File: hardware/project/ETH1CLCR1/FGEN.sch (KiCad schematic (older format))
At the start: 74 parts, among them U801 ECS-3225SMV-500-GP-TR, U802 REF192, U803 74AHCT1G08, U804 AD5689BRUZ, U805 AD9835, U806 TL072, U807 DG419LDY, U808 AD5453YRMZ, U809 LT1468, U810 LT1468, U811 LT1468

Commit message: PCB layout
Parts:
- added C832, C833, C835: 100n, Capacitor_SMD:C_0603_1608Metric_Pad1.05x0.95mm_HandSolder, symbol Device:C
- renumbered C832 to C834
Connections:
- net +15VF: now also C832.1, C835.1
- net -15VF: now also C833.1
- net AGNDF: now also C832.2, C833.2, C835.2
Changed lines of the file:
@@
 NoConn ~ 10650 2200
 $Comp
-L ETH1CLCR1:-15VF #PWR0871
+L ETH1CLCR1:-15VF #PWR0873
 U 1 1 5DDED26A
 P 10450 2300
-F 0 "#PWR0871" H 10450 2150 50  0001 C CNN
+F 0 "#PWR0873" H 10450 2150 50  0001 C CNN
 F 1 "-15VF" H 10465 2473 50  0000 C CNN
 F 2 "" H 10450 2300 50  0001 C CNN
@@
 	10000 1200 11100 1200
 $Comp
-L ETH1CLCR1:+15VF #PWR0873
+L ETH1CLCR1:+15VF #PWR0877
 U 1 1 5DE564DC
 P 12000 1600
-F 0 "#PWR0873" H 12000 1450 50  0001 C CNN
+F 0 "#PWR0877" H 12000 1450 50  0001 C CNN
 F 1 "+15VF" H 12015 1773 50  0000 C CNN
 F 2 "" H 12000 1600 50  0001 C CNN
@@
 $EndComp
 $Comp
-L ETH1CLCR1:-15VF #PWR0874
+L ETH1CLCR1:-15VF #PWR0878
 U 1 1 5DE5674F
 P 12000 2400
-F 0 "#PWR0874" H 12000 2250 50  0001 C CNN
+F 0 "#PWR0878" H 12000 2250 50  0001 C CNN
 F 1 "-15VF" H 12015 2573 50  0000 C CNN
 F 2 "" H 12000 2400 50  0001 C CNN
@@
 	12550 2000 12500 2000
 $Comp
-L Device:C C832
+L Device:C C834
 U 1 1 5E0264FF
 P 12050 850
-F 0 "C832" V 11798 850 50  0000 C CNN
+F 0 "C834" V 11798 850 50  0000 C CNN
 F 1 "C" V 11889 850 50  0000 C CNN
 F 2 "Capacitor_SMD:C_0603_1608Metric_Pad1.05x0.95mm_HandSolder" H 12088 700 50  0001 C CNN
@@
 	3150 1700 3200 1700
 $Comp
-L ETH1CLCR1:AGNDF #PWR0872
+L ETH1CLCR1:AGNDF #PWR0876
 U 1 1 5E27881E
 P 11650 2100
-F 0 "#PWR0872" H 11650 1850 50  0001 C CNN
+F 0 "#PWR0876" H 11650 1850 50  0001 C CNN
 F 1 "AGNDF" V 11655 1972 50  0000 R CNN
 F 2 "" H 11650 2100 50  0001 C CNN
@@
 	14700 2850 14700 2400
 $Comp
-L ETH1CLCR1:+15VF #PWR0870
+L ETH1CLCR1:+15VF #PWR0872
 U 1 1 5DDEC9BC
 P 10450 1500
-F 0 "#PWR0870" H 10450 1350 50  0001 C CNN
+F 0 "#PWR0872" H 10450 1350 50  0001 C CNN
 F 1 "+15VF" H 10465 1673 50  0000 C CNN
 F 2 "" H 10450 1500 50  0001 C CNN
@@
 $EndComp
 $Comp
-L ETH1CLCR1:+15VF #PWR0876
+L ETH1CLCR1:+15VF #PWR0880
 U 1 1 5E35B1C8
 P 13750 1700
-F 0 "#PWR0876" H 13750 1550 50  0001 C CNN
+F 0 "#PWR0880" H 13750 1550 50  0001 C CNN
 F 1 "+15VF" H 13765 1873 50  0000 C CNN
 F 2 "" H 13750 1700 50  0001 C CNN
@@
 $EndComp
 $Comp
-L ETH1CLCR1:-15VF #PWR0877
+L ETH1CLCR1:-15VF #PWR0881
 U 1 1 5E35B1CE
 P 13750 2500
-F 0 "#PWR0877" H 13750 2350 50  0001 C CNN
+F 0 "#PWR0881" H 13750 2350 50  0001 C CNN
 F 1 "-15VF" H 13765 2673 50  0000 C CNN
 F 2 "" H 13750 2500 50  0001 C CNN
@@
 	14350 2100 14250 2100
 $Comp
-L ETH1CLCR1:AGNDF #PWR0875
+L ETH1CLCR1:AGNDF #PWR0879
 U 1 1 5E35B1F0
 P 13400 2200
-F 0 "#PWR0875" H 13400 1950 50  0001 C CNN
+F 0 "#PWR0879" H 13400 1950 50  0001 C CNN
 F 1 "AGNDF" V 13405 2072 50  0000 R CNN
 F 2 "" H 13400 2200 50  0001 C CNN
@@
 $EndComp
 $Comp
-L ETH1CLCR1:AGNDF #PWR0878
+L ETH1CLCR1:AGNDF #PWR0882
 U 1 1 5DE80F16
 P 15400 2000
-F 0 "#PWR0878" H 15400 1750 50  0001 C CNN
+F 0 "#PWR0882" H 15400 1750 50  0001 C CNN
 F 1 "AGNDF" V 15400 1750 50  0000 C CNN
 F 2 "" H 15400 2000 50  0001 C CNN
@@
 Wire Wire Line
 	15400 2000 15350 2000
+$Comp
+L ETH1CLCR1:-15VF #PWR0874
+U 1 1 5E24F356
+P 10600 9750
+F 0 "#PWR0874" H 10600 9600 50  0001 C CNN
+F 1 "-15VF" H 10615 9923 50  0000 C CNN
+F 2 "" H 10600 9750 50  0001 C CNN
+F 3 "" H 10600 9750 50  0001 C CNN
+	1    10600 9750
+	1    0    0    -1
+$EndComp
+Wire Wire Line
+	10600 9950 10600 9750
+Wire Wire Line
+	10600 10450 10600 10250
+$Comp
+L ETH1CLCR1:AGNDF #PWR0875
+U 1 1 5E24F35E
+P 10600 10450
+F 0 "#PWR0875" H 10600 10200 50  0001 C CNN
+F 1 "AGNDF" H 10605 10277 50  0000 C CNN
+F 2 "" H 10600 10450 50  0001 C CNN
+F 3 "" H 10600 10450 50  0001 C CNN
+	1    10600 10450
+	1    0    0    -1
+$EndComp
+$Comp
+L Device:C C833
+U 1 1 5E24F364
+P 10600 10100
+F 0 "C833" H 10715 10146 50  0000 L CNN
+F 1 "100n" H 10715 10055 50  0000 L CNN
+F 2 "Capacitor_SMD:C_0603_1608Metric_Pad1.05x0.95mm_HandSolder" H 10638 9950 50  0001 C CNN
+F 3 "~" H 10600 10100 50  0001 C CNN
+	1    10600 10100
+	1    0    0    -1
+$EndComp
+Wire Wire Line
+	10050 9950 10050 9750
+Wire Wire Line
+	10050 10450 10050 10250
+$Comp
+L ETH1CLCR1:AGNDF #PWR0871
+U 1 1 5E24F36C
+P 10050 10450
+F 0 "#PWR0871" H 10050 10200 50  0001 C CNN
+F 1 "AGNDF" H 10055 10277 50  0000 C CNN
+F 2 "" H 10050 10450 50  0001 C CNN
+F 3 "" H 10050 10450 50  0001 C CNN
+	1    10050 10450
+	1    0    0    -1
+$EndComp
+$Comp
+L Device:C C832
+U 1 1 5E24F372
+P 10050 10100
+F 0 "C832" H 10165 10146 50  0000 L CNN
+F 1 "100n" H 10165 10055 50  0000 L CNN
+F 2 "Capacitor_SMD:C_0603_1608Metric_Pad1.05x0.95mm_HandSolder" H 10088 9950 50  0001 C CNN
+F 3 "~" H 10050 10100 50  0001 C CNN
+	1    10050 10100
+	1    0    0    -1
+$EndComp
+$Comp
+L ETH1CLCR1:+15VF #PWR0870
+U 1 1 5E24F378
+P 10050 9750
+F 0 "#PWR0870" H 10050 9600 50  0001 C CNN
+F 1 "+15VF" H 10065 9923 50  0000 C CNN
+F 2 "" H 10050 9750 50  0001 C CNN
+F 3 "" H 10050 9750 50  0001 C CNN
+	1    10050 9750
+	1    0    0    -1
+$EndComp
+Wire Wire Line
+	11100 9950 11100 9750
+Wire Wire Line
+	11100 10400 11100 10250
+$Comp
+L ETH1CLCR1:AGNDF #PWR0884
+U 1 1 5E2BFE2B
+P 11100 10400
+F 0 "#PWR0884" H 11100 10150 50  0001 C CNN
+F 1 "AGNDF" H 11105 10227 50  0000 C CNN
+F 2 "" H 11100 10400 50  0001 C CNN
+F 3 "" H 11100 10400 50  0001 C CNN
+	1    11100 10400
+	1    0    0    -1
+$EndComp
+$Comp
+L Device:C C835
+U 1 1 5E2BFE31
+P 11100 10100
+F 0 "C835" H 11215 10146 50  0000 L CNN
+F 1 "100n" H 11215 10055 50  0000 L CNN
+F 2 "Capacitor_SMD:C_0603_1608Metric_Pad1.05x0.95mm_HandSolder" H 11138 9950 50  0001 C CNN
+F 3 "~" H 11100 10100 50  0001 C CNN
+	1    11100 10100
+	1    0    0    -1
+$EndComp
+$Comp
+L ETH1CLCR1:+15VF #PWR0883
+U 1 1 5E2BFE37
+P 11100 9750
+F 0 "#PWR0883" H 11100 9600 50  0001 C CNN
+F 1 "+15VF" H 11115 9923 50  0000 C CNN
+F 2 "" H 11100 9750 50  0001 C CNN
+F 3 "" H 11100 9750 50  0001 C CNN
+	1    11100 9750
+	1    0    0    -1
+$EndComp
 $EndSCHEMATC

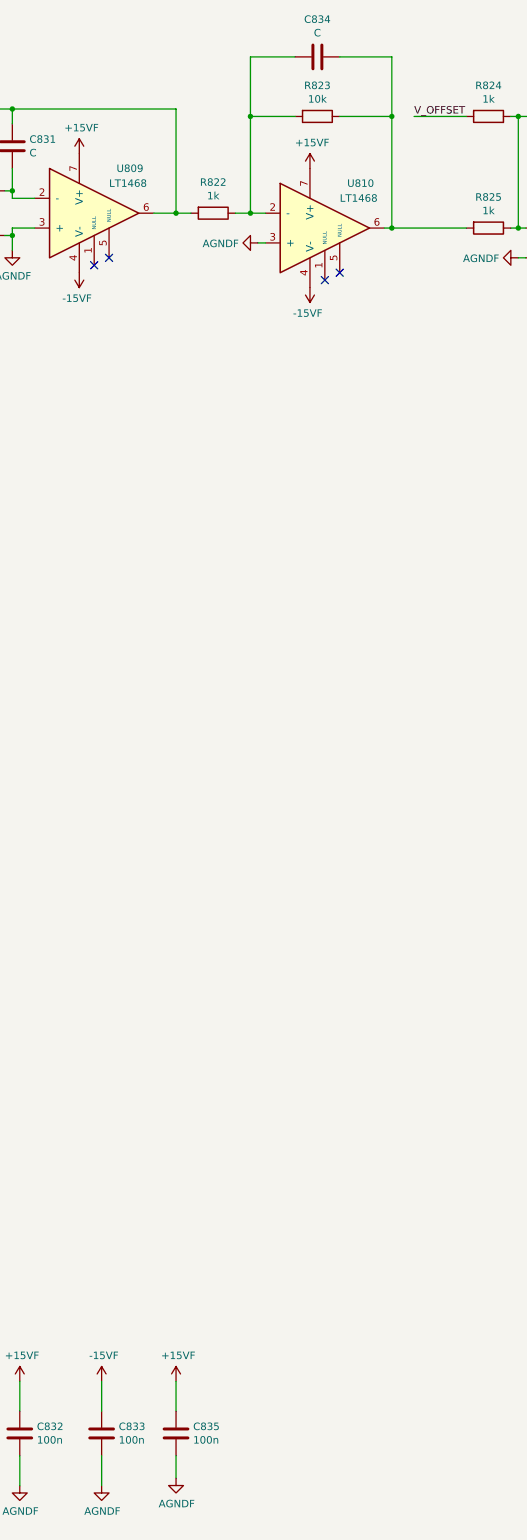
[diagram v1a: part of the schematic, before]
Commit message: Redesinged ADC schematic.
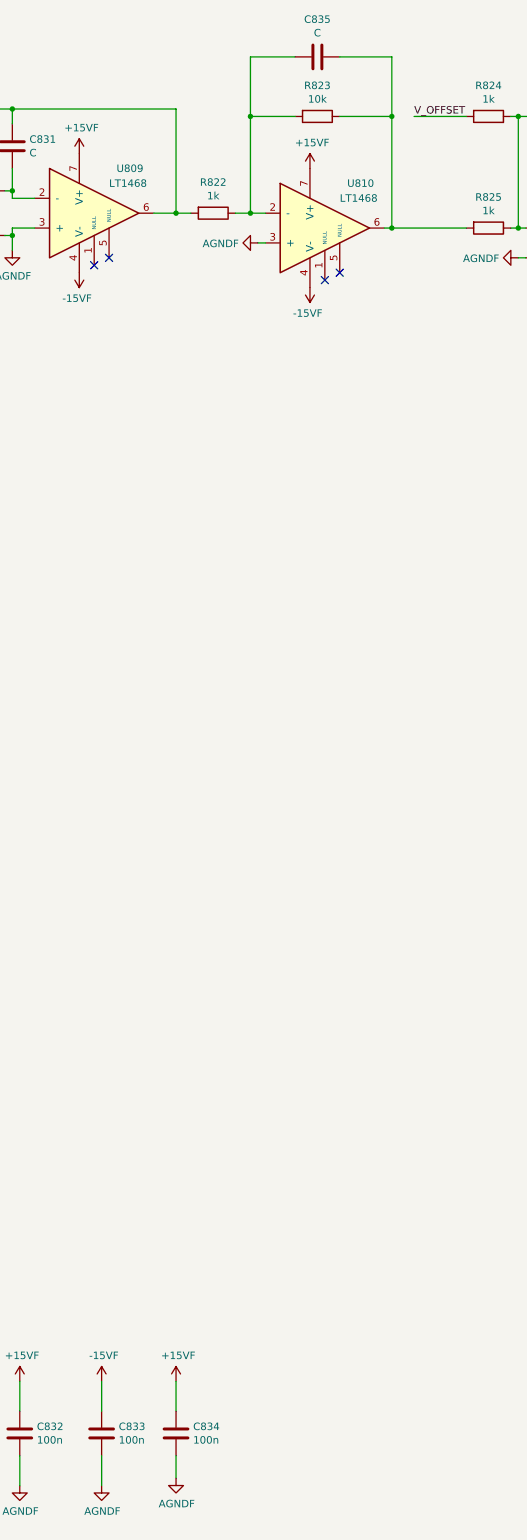
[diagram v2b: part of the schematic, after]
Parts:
- renumbered C835 to C834, C834 to C835
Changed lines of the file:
@@
 	10000 1200 11100 1200
 $Comp
-L ETH1CLCR1:+15VF #PWR0877
+L ETH1CLCR1:+15VF #PWR0879
 U 1 1 5DE564DC
 P 12000 1600
-F 0 "#PWR0877" H 12000 1450 50  0001 C CNN
+F 0 "#PWR0879" H 12000 1450 50  0001 C CNN
 F 1 "+15VF" H 12015 1773 50  0000 C CNN
 F 2 "" H 12000 1600 50  0001 C CNN
@@
 $EndComp
 $Comp
-L ETH1CLCR1:-15VF #PWR0878
+L ETH1CLCR1:-15VF #PWR0880
 U 1 1 5DE5674F
 P 12000 2400
-F 0 "#PWR0878" H 12000 2250 50  0001 C CNN
+F 0 "#PWR0880" H 12000 2250 50  0001 C CNN
 F 1 "-15VF" H 12015 2573 50  0000 C CNN
 F 2 "" H 12000 2400 50  0001 C CNN
@@
 	12550 2000 12500 2000
 $Comp
-L Device:C C834
+L Device:C C835
 U 1 1 5E0264FF
 P 12050 850
-F 0 "C834" V 11798 850 50  0000 C CNN
+F 0 "C835" V 11798 850 50  0000 C CNN
 F 1 "C" V 11889 850 50  0000 C CNN
 F 2 "Capacitor_SMD:C_0603_1608Metric_Pad1.05x0.95mm_HandSolder" H 12088 700 50  0001 C CNN
@@
 	3150 1700 3200 1700
 $Comp
-L ETH1CLCR1:AGNDF #PWR0876
+L ETH1CLCR1:AGNDF #PWR0878
 U 1 1 5E27881E
 P 11650 2100
-F 0 "#PWR0876" H 11650 1850 50  0001 C CNN
+F 0 "#PWR0878" H 11650 1850 50  0001 C CNN
 F 1 "AGNDF" V 11655 1972 50  0000 R CNN
 F 2 "" H 11650 2100 50  0001 C CNN
@@
 $EndComp
 $Comp
-L ETH1CLCR1:+15VF #PWR0880
+L ETH1CLCR1:+15VF #PWR0882
 U 1 1 5E35B1C8
 P 13750 1700
-F 0 "#PWR0880" H 13750 1550 50  0001 C CNN
+F 0 "#PWR0882" H 13750 1550 50  0001 C CNN
 F 1 "+15VF" H 13765 1873 50  0000 C CNN
 F 2 "" H 13750 1700 50  0001 C CNN
@@
 $EndComp
 $Comp
-L ETH1CLCR1:-15VF #PWR0881
+L ETH1CLCR1:-15VF #PWR0883
 U 1 1 5E35B1CE
 P 13750 2500
-F 0 "#PWR0881" H 13750 2350 50  0001 C CNN
+F 0 "#PWR0883" H 13750 2350 50  0001 C CNN
 F 1 "-15VF" H 13765 2673 50  0000 C CNN
 F 2 "" H 13750 2500 50  0001 C CNN
@@
 	14350 2100 14250 2100
 $Comp
-L ETH1CLCR1:AGNDF #PWR0879
+L ETH1CLCR1:AGNDF #PWR0881
 U 1 1 5E35B1F0
 P 13400 2200
-F 0 "#PWR0879" H 13400 1950 50  0001 C CNN
+F 0 "#PWR0881" H 13400 1950 50  0001 C CNN
 F 1 "AGNDF" V 13405 2072 50  0000 R CNN
 F 2 "" H 13400 2200 50  0001 C CNN
@@
 $EndComp
 $Comp
-L ETH1CLCR1:AGNDF #PWR0882
+L ETH1CLCR1:AGNDF #PWR0884
 U 1 1 5DE80F16
 P 15400 2000
-F 0 "#PWR0882" H 15400 1750 50  0001 C CNN
+F 0 "#PWR0884" H 15400 1750 50  0001 C CNN
 F 1 "AGNDF" V 15400 1750 50  0000 C CNN
 F 2 "" H 15400 2000 50  0001 C CNN
@@
 	11100 10400 11100 10250
 $Comp
-L ETH1CLCR1:AGNDF #PWR0884
+L ETH1CLCR1:AGNDF #PWR0877
 U 1 1 5E2BFE2B
 P 11100 10400
-F 0 "#PWR0884" H 11100 10150 50  0001 C CNN
+F 0 "#PWR0877" H 11100 10150 50  0001 C CNN
 F 1 "AGNDF" H 11105 10227 50  0000 C CNN
 F 2 "" H 11100 10400 50  0001 C CNN
@@
 $EndComp
 $Comp
-L Device:C C835
+L Device:C C834
 U 1 1 5E2BFE31
 P 11100 10100
-F 0 "C835" H 11215 10146 50  0000 L CNN
+F 0 "C834" H 11215 10146 50  0000 L CNN
 F 1 "100n" H 11215 10055 50  0000 L CNN
 F 2 "Capacitor_SMD:C_0603_1608Metric_Pad1.05x0.95mm_HandSolder" H 11138 9950 50  0001 C CNN
@@
 $EndComp
 $Comp
-L ETH1CLCR1:+15VF #PWR0883
+L ETH1CLCR1:+15VF #PWR0876
 U 1 1 5E2BFE37
 P 11100 9750
-F 0 "#PWR0883" H 11100 9600 50  0001 C CNN
+F 0 "#PWR0876" H 11100 9600 50  0001 C CNN
 F 1 "+15VF" H 11115 9923 50  0000 C CNN
 F 2 "" H 11100 9750 50  0001 C CNN

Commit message: Redesigned the power supply, added humidy+temp. sensor.
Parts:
- renumbered C801 to C1401, C802 to C1402, C803 to C1403, C804 to C1404, C805 to C1405, C806 to C1406, C807 to C1407, C808 to C1408, C809 to C1409, C810 to C1410, C811 to C1411, C812 to C1412, C813 to C1413, C814 to C1414, C815 to C1415, C816 to C1416, C817 to C1417, C818 to C1418, C819 to C1419, C820 to C1420, C821 to C1421, C822 to C1422, C823 to C1423, C824 to C1424, C825 to C1425, C826 to C1426, C827 to C1427, C828 to C1428, C829 to C1429, C830 to C1430, C831 to C1431, C832 to C1432, C833 to C1433, C834 to C1434, C835 to C1435, D801 to D1401, L801 to L1401, L802 to L1402, L803 to L1403, R801 to R1401, R802 to R1402, R803 to R1403, R804 to R1404, R805 to R1405, R806 to R1406, R807 to R1407, R808 to R1408, R809 to R1409, R810 to R1410, R811 to R1411, R812 to R1412, R813 to R1413, R814 to R1414, R815 to R1415, R816 to R1416, R817 to R1417, R818 to R1418, R819 to R1419, R820 to R1420, R821 to R1421, R822 to R1422, R823 to R1423, R824 to R1424, R825 to R1425, R826 to R1426, R827 to R1427, U801 to U1401, U802 to U1402, U803 to U1403, U804 to U1404, U805 to U1405, U806 to U1406, U807 to U1407, U808 to U1408, U809 to U1409, U810 to U1410, U811 to U1411

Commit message: Checked the schematics. Created BOM.
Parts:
- removed C1433, C1434: 100n, Capacitor_SMD:C_0603_1608Metric_Pad1.05x0.95mm_HandSolder, symbol Device:C
- added C1410: 100n, Capacitor_SMD:C_0603_1608Metric_Pad1.05x0.95mm_HandSolder, symbol Device:C
- added C1417: 10n, Capacitor_SMD:C_0603_1608Metric_Pad1.05x0.95mm_HandSolder, symbol Device:C
- added C1435: 10u, Capacitor_SMD:C_0805_2012Metric_Pad1.15x1.40mm_HandSolder, symbol Device:C
- added R1422: DNP, Resistor_SMD:R_0603_1608Metric_Pad1.05x0.95mm_HandSolder, symbol Device:R
- C1434: renamed from C1431; value C -> 1p5
- C1436: renamed from C1435; value C -> 1p5
- R1403, R1404: value NC -> DNP
- R1420, R1421: value R -> 0
- R1428: renamed from R1427; value R -> DNP
- renumbered C1403 to C1402, C1402 to C1403, C1406 to C1405, C1405 to C1406, C1410 to C1412, C1414 to C1413, C1412 to C1414, C1413 to C1416, C1416 to C1418, C1417 to C1419, C1418 to C1420, C1419 to C1421, C1420 to C1422, C1422 to C1423, C1421 to C1424, C1423 to C1425, C1425 to C1426, C1424 to C1427, C1426 to C1428, C1427 to C1429, C1429 to C1430, C1428 to C1431, C1430 to C1432, C1432 to C1433, R1409 to R1407, R1407 to R1408, R1408 to R1409, R1413 to R1411, R1411 to R1412, R1412 to R1413, R1422 to R1423, R1423 to R1424, R1424 to R1425, R1425 to R1426, R1426 to R1427
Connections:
- net +3.3VF: now also C1435.1
- net AGNDF: now also C1410.2, C1417.2, C1435.2
- net at R1411.1, U1405.1 (FSADJ): now also C1410.1
- net at U1405.3 (REFOUT): now also C1417.1
- net at R1420.1, U1408.7 (VREF): now also R1422.2
- net at C1436.2, R1423.1, R1424.2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: now also R1422.1
- no-connect marks 9 -> 8
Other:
- moved on the sheet: C1403, C1406, C1412, C1413, C1414, C1416, C1418, C1419, C1420, C1421, C1422, C1424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

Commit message: PCB layout
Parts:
- added C1437, C1438: 100n, Capacitor_SMD:C_0603_1608Metric_Pad1.05x0.95mm_HandSolder, symbol Device:C
- R1428: value DNP -> 10k
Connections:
- net +2V5REF: now also C1438.1
- net +3.3VF: now also C1437.1
- net AGNDF: now also C1437.2, C1438.2
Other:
- moved on the sheet: C1401, C1402, C1403, C1404, C1405, C1406, C1407, C1408, C1409, C1411, C1412, C1414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

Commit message: PCB done.
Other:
- moved on the sheet: C1403, C1406, C1407, C1412, C1414, C1416, C1419, C1438, D1401A, D1401B, R1401, R1402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

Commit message: Bug fixes in FGEN schematic. Software for AD9835 and AD5689 works.
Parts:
- R1422: value DNP -> 10k
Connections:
- net +3.3VF: no longer U1401.1 (EN)
- no-connect marks 8 -> 9
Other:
- moved on the sheet: C1403, C1406, C1407, C1410, C1412, C1413, C1414, C1416, C1417, C1418, C1419, C1420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
